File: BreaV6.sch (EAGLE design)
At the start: 34 parts, among them J1 XF2L-0535-1, J2 XF2L-0535-1, Q1 ABM-16MHZ, SW1 LS12T2-T, SW2 EVQ11U09K, SW3 ESE31L11T, U2 TPS62200, X1 22-23-2021

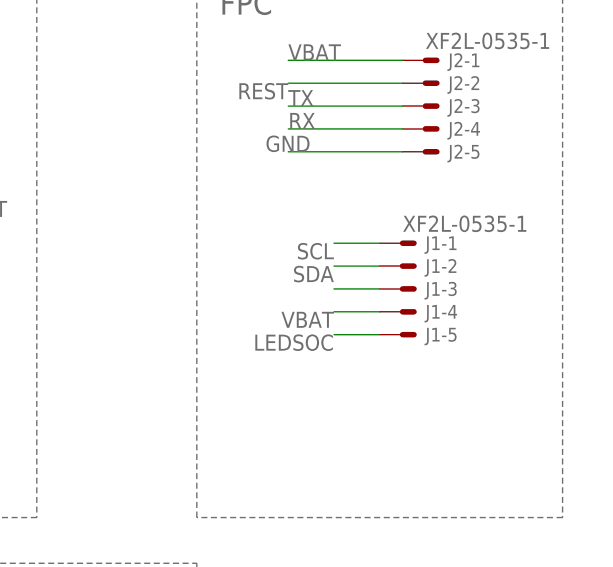
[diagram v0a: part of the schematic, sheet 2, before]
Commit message: Brea V6   PwrSW and DetSW swap
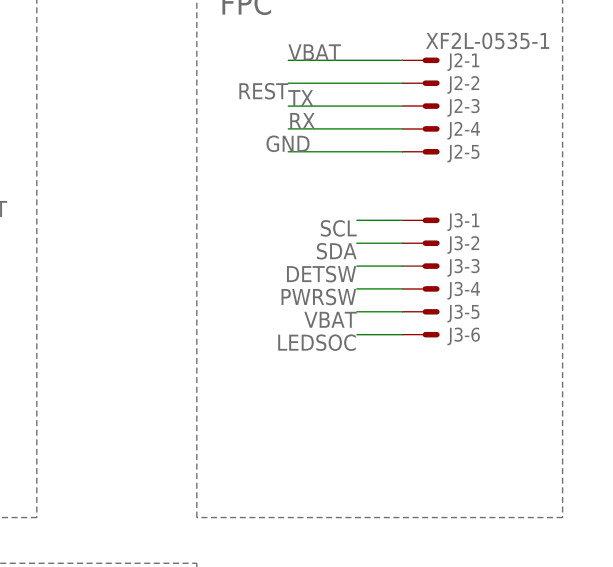
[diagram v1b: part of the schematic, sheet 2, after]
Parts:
- removed J1: XF2L-0535-1, adafruit:XF2L-0535-1
- added J3: XF2L-0635-1, con-omron:XF2L-0635-1
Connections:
- removed net N$6: J1-3.MS
- net DETSW: now also J3-3.MS, U1.PD2(INT0)
- net LEDSOC: now also J3-6.MS; no longer J1-5.MS
- net PWRSW: now also J3-4.MS, U1.PD3(INT1); no longer U1.PD2(INT0)
- net SCL: now also J3-1.MS; no longer J1-1.MSV
- net SDA: now also J3-2.MS; no longer J1-2.MS
- net VBAT: now also J3-5.MS; no longer J1-4.MS
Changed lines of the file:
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@@
 <part name="J2" library="adafruit" deviceset="XF2*-05?" device="35-1" technology="L"/>
 <part name="X1" library="con-molex" deviceset="22-23-2021" device=""/>
-<part name="J1" library="adafruit" deviceset="XF2*-05?" device="35-1" technology="L"/>
 <part name="SW3" library="NewPart" deviceset="ESE31L11T" device=""/>
 <part name="SW2" library="NewPart" deviceset="EVQ11U09K" device=""/>
@@
 <part name="D2" library="diode" library_urn="urn:adsk.eagle:library:210" deviceset="DIODE-" device="SOD523" package3d_urn="urn:adsk.eagle:package:43410/1"/>
 <part name="D3" library="diode" library_urn="urn:adsk.eagle:library:210" deviceset="DIODE-" device="SOD523" package3d_urn="urn:adsk.eagle:package:43410/1"/>
+<part name="J3" library="con-omron" library_urn="urn:adsk.eagle:library:167" deviceset="XF2*-06?" device="35-1" package3d_urn="urn:adsk.eagle:package:9024/1" technology="L"/>
 </parts>
 <sheets>
@@
 </segment>
 </net>
-<net name="PWRSW" class="0">
+<net name="LEDSOC" class="0">
+<segment>
+<pinref part="U1" gate="U$1" pin="PD4(XCK/T0)"/>
+<wire x1="86.36" y1="48.26" x2="91.44" y2="48.26" width="0.1524" layer="91"/>
+<label x="91.44" y="48.26" size="1.778" layer="95"/>
+</segment>
+</net>
+<net name="DETSW" class="0">
 <segment>
 <pinref part="U1" gate="U$1" pin="PD2(INT0)"/>
@@
 </segment>
 </net>
-<net name="LEDSOC" class="0">
-<segment>
-<pinref part="U1" gate="U$1" pin="PD4(XCK/T0)"/>
-<wire x1="86.36" y1="48.26" x2="91.44" y2="48.26" width="0.1524" layer="91"/>
-<label x="91.44" y="48.26" size="1.778" layer="95"/>
+<net name="PWRSW" class="0">
+<segment>
+<pinref part="U1" gate="U$1" pin="PD3(INT1)"/>
+<wire x1="86.36" y1="50.8" x2="91.44" y2="50.8" width="0.1524" layer="91"/>
+<label x="91.44" y="50.8" size="1.778" layer="95"/>
 </segment>
 </net>
@@
 <instance part="X1" gate="-1" x="60.96" y="17.78"/>
 <instance part="X1" gate="-2" x="60.96" y="15.24"/>
-<instance part="J1" gate="-1" x="160.02" y="78.74"/>
-<instance part="J1" gate="-2" x="160.02" y="76.2"/>
-<instance part="J1" gate="-3" x="160.02" y="73.66"/>
-<instance part="J1" gate="-4" x="160.02" y="71.12"/>
-<instance part="J1" gate="-5" x="160.02" y="68.58"/>
 <instance part="GND12" gate="1" x="109.22" y="5.08"/>
 <instance part="R7" gate="G$1" x="109.22" y="25.4" rot="R270"/>
@@
 <instance part="D2" gate="G$1" x="15.24" y="27.94"/>
 <instance part="D3" gate="G$1" x="15.24" y="17.78"/>
+<instance part="J3" gate="-1" x="162.56" y="81.28"/>
+<instance part="J3" gate="-2" x="162.56" y="78.74"/>
+<instance part="J3" gate="-3" x="162.56" y="76.2"/>
+<instance part="J3" gate="-4" x="162.56" y="73.66"/>
+<instance part="J3" gate="-5" x="162.56" y="71.12"/>
+<instance part="J3" gate="-6" x="162.56" y="68.58"/>
 </instances>
 <busses>
@@
 <label x="40.64" y="25.4" size="1.778" layer="95"/>
 </segment>
+<segment>
+<pinref part="J3" gate="-4" pin="MS"/>
+<wire x1="160.02" y1="73.66" x2="154.94" y2="73.66" width="0.1524" layer="91"/>
+<label x="154.94" y="73.66" size="1.778" layer="95" rot="R180"/>
+</segment>
 </net>
 <net name="N$5" class="0">
@@
 <label x="147.32" y="96.52" size="1.778" layer="95" rot="R180"/>
 <pinref part="J2" gate="-2" pin="MS"/>
-</segment>
-</net>
-<net name="SDA" class="0">
-<segment>
-<wire x1="157.48" y1="76.2" x2="152.4" y2="76.2" width="0.1524" layer="91"/>
-<label x="152.4" y="76.2" size="1.778" layer="95" rot="R180"/>
-<pinref part="J1" gate="-2" pin="MS"/>
-</segment>
-</net>
-<net name="SCL" class="0">
-<segment>
-<wire x1="157.48" y1="78.74" x2="152.4" y2="78.74" width="0.1524" layer="91"/>
-<label x="152.4" y="78.74" size="1.778" layer="95" rot="R180"/>
-<pinref part="J1" gate="-1" pin="MSV"/>
 </segment>
 </net>
@@
 <label x="109.22" y="30.48" size="1.778" layer="95" rot="R180" xref="yes"/>
 </segment>
+<segment>
+<pinref part="J3" gate="-3" pin="MS"/>
+<wire x1="160.02" y1="76.2" x2="154.94" y2="76.2" width="0.1524" layer="91"/>
+<label x="154.94" y="76.2" size="1.778" layer="95" rot="R180"/>
+</segment>
 </net>
 <net name="RX" class="0">
@@
 <net name="LEDSOC" class="0">
 <segment>
-<pinref part="J1" gate="-5" pin="MS"/>
-<wire x1="157.48" y1="68.58" x2="152.4" y2="68.58" width="0.1524" layer="91"/>
-<label x="152.4" y="68.58" size="1.778" layer="95" rot="R180"/>
+<pinref part="J3" gate="-6" pin="MS"/>
+<wire x1="160.02" y1="68.58" x2="154.94" y2="68.58" width="0.1524" layer="91"/>
+<label x="154.94" y="68.58" size="1.778" layer="95" rot="R180"/>
 </segment>
 </net>
 <net name="VBAT" class="0">
-<segment>
-<pinref part="J1" gate="-4" pin="MS"/>
-<wire x1="157.48" y1="71.12" x2="152.4" y2="71.12" width="0.1524" layer="91"/>
-<label x="152.4" y="71.12" size="1.778" layer="95" rot="R180"/>
-</segment>
 <segment>
 <pinref part="J2" gate="-1" pin="MSV"/>
@@
 <wire x1="12.7" y1="17.78" x2="7.62" y2="17.78" width="0.1524" layer="91"/>
 <label x="7.62" y="17.78" size="1.778" layer="95" rot="R180" xref="yes"/>
+</segment>
+<segment>
+<pinref part="J3" gate="-5" pin="MS"/>
+<wire x1="160.02" y1="71.12" x2="154.94" y2="71.12" width="0.1524" layer="91"/>
+<label x="154.94" y="71.12" size="1.778" layer="95" rot="R180"/>
 </segment>
 </net>
@@
 </segment>
 </net>
-<net name="N$6" class="0">
-<segment>
-<pinref part="J1" gate="-3" pin="MS"/>
-<wire x1="157.48" y1="73.66" x2="152.4" y2="73.66" width="0.1524" layer="91"/>
-</segment>
-</net>
+<net name="SCL" class="0">
+<segment>
+<pinref part="J3" gate="-1" pin="MS"/>
+<wire x1="160.02" y1="81.28" x2="154.94" y2="81.28" width="0.1524" layer="91"/>
+<label x="154.94" y="81.28" size="1.778" layer="95" rot="R180"/>
+</segment>
+</net>
+<net name="SDA" class="0">
+<segment>
+<pinref part="J3" gate="-2" pin="MS"/>
+<wire x1="160.02" y1="78.74" x2="154.94" y2="78.74" width="0.1524" layer="91"/>
+<label x="154.94" y="78.74" size="1.778" layer="95" rot="R180"/>
+</segment>
+</net>

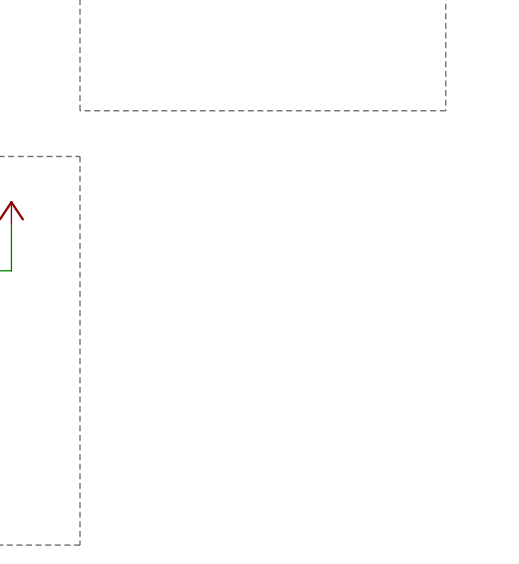
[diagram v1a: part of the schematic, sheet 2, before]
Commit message: To add signal control
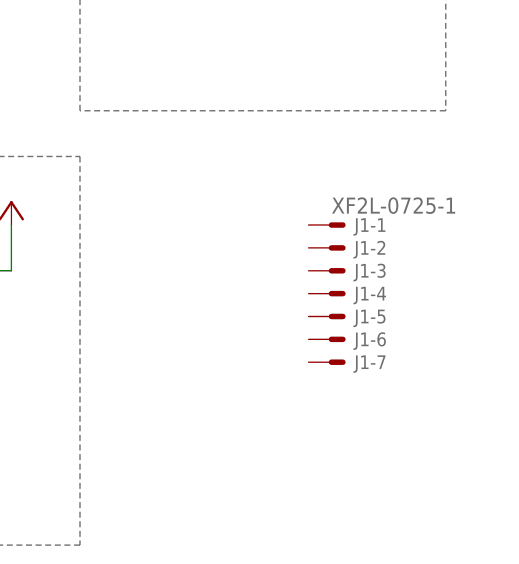
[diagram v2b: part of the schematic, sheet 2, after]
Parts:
- added J1: XF2L-0725-1, con-omron:XF2L-0725-1
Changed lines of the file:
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@@
 <part name="D3" library="diode" library_urn="urn:adsk.eagle:library:210" deviceset="DIODE-" device="SOD523" package3d_urn="urn:adsk.eagle:package:43410/1"/>
 <part name="J3" library="con-omron" library_urn="urn:adsk.eagle:library:167" deviceset="XF2*-06?" device="35-1" package3d_urn="urn:adsk.eagle:package:9024/1" technology="L"/>
+<part name="J1" library="con-omron" library_urn="urn:adsk.eagle:library:167" deviceset="XF2*-07?" device="25-1" package3d_urn="urn:adsk.eagle:package:9008/1" technology="L"/>
 </parts>
 <sheets>
@@
 <instance part="J3" gate="-5" x="162.56" y="71.12"/>
 <instance part="J3" gate="-6" x="162.56" y="68.58"/>
+<instance part="J1" gate="-1" x="165.1" y="35.56"/>
+<instance part="J1" gate="-2" x="165.1" y="33.02"/>
+<instance part="J1" gate="-3" x="165.1" y="30.48"/>
+<instance part="J1" gate="-4" x="165.1" y="27.94"/>
+<instance part="J1" gate="-5" x="165.1" y="25.4"/>
+<instance part="J1" gate="-6" x="165.1" y="22.86"/>
+<instance part="J1" gate="-7" x="165.1" y="20.32"/>
 </instances>
 <busses>

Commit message: Final board files
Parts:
- removed J1: XF2L-0725-1, con-omron:XF2L-0725-1
- added X2: CON-1PINB, NewPart:CON-1PINB
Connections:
- new net SHUTDOWN_SIG: J3-6.MS, U1.PD4(XCK/T0)
- net LEDSOC: now also U1.PD5(T1), X2.P$1; no longer J3-6.MS, U1.PD4(XCK/T0)
- net REST: now also U1.PD6(AIN0); no longer U1.PD5(T1)
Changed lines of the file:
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@@
 <part name="D3" library="diode" library_urn="urn:adsk.eagle:library:210" deviceset="DIODE-" device="SOD523" package3d_urn="urn:adsk.eagle:package:43410/1"/>
 <part name="J3" library="con-omron" library_urn="urn:adsk.eagle:library:167" deviceset="XF2*-06?" device="35-1" package3d_urn="urn:adsk.eagle:package:9024/1" technology="L"/>
-<part name="J1" library="con-omron" library_urn="urn:adsk.eagle:library:167" deviceset="XF2*-07?" device="25-1" package3d_urn="urn:adsk.eagle:package:9008/1" technology="L"/>
+<part name="X2" library="NewPart" deviceset="CON-1PINB" device=""/>
 </parts>
 <sheets>
@@
 </segment>
 </net>
-<net name="REST" class="0">
-<segment>
-<pinref part="U1" gate="U$1" pin="PD5(T1)"/>
-<wire x1="86.36" y1="45.72" x2="93.98" y2="45.72" width="0.1524" layer="91"/>
-<label x="93.98" y="45.72" size="1.778" layer="95"/>
-</segment>
-</net>
 <net name="RX" class="0">
 <segment>
@@
 </segment>
 </net>
-<net name="LEDSOC" class="0">
+<net name="SHUTDOWN_SIG" class="0">
 <segment>
 <pinref part="U1" gate="U$1" pin="PD4(XCK/T0)"/>
@@
 <wire x1="86.36" y1="50.8" x2="91.44" y2="50.8" width="0.1524" layer="91"/>
 <label x="91.44" y="50.8" size="1.778" layer="95"/>
+</segment>
+</net>
+<net name="REST" class="0">
+<segment>
+<pinref part="U1" gate="U$1" pin="PD6(AIN0)"/>
+<wire x1="86.36" y1="43.18" x2="91.44" y2="43.18" width="0.1524" layer="91"/>
+<label x="91.44" y="43.18" size="1.778" layer="95"/>
+</segment>
+</net>
+<net name="LEDSOC" class="0">
+<segment>
+<pinref part="U1" gate="U$1" pin="PD5(T1)"/>
+<wire x1="86.36" y1="45.72" x2="91.44" y2="45.72" width="0.1524" layer="91"/>
+<label x="91.44" y="45.72" size="1.778" layer="95"/>
 </segment>
 </net>
@@
 <instance part="J3" gate="-5" x="162.56" y="71.12"/>
 <instance part="J3" gate="-6" x="162.56" y="68.58"/>
-<instance part="J1" gate="-1" x="165.1" y="35.56"/>
-<instance part="J1" gate="-2" x="165.1" y="33.02"/>
-<instance part="J1" gate="-3" x="165.1" y="30.48"/>
-<instance part="J1" gate="-4" x="165.1" y="27.94"/>
-<instance part="J1" gate="-5" x="165.1" y="25.4"/>
-<instance part="J1" gate="-6" x="165.1" y="22.86"/>
-<instance part="J1" gate="-7" x="165.1" y="20.32"/>
+<instance part="X2" gate="G$1" x="165.1" y="58.42"/>
 </instances>
 <busses>
@@
 </segment>
 </net>
-<net name="LEDSOC" class="0">
+<net name="SHUTDOWN_SIG" class="0">
 <segment>
 <pinref part="J3" gate="-6" pin="MS"/>
@@
 </segment>
 </net>
+<net name="LEDSOC" class="0">
+<segment>
+<pinref part="X2" gate="G$1" pin="P$1"/>
+<wire x1="160.02" y1="58.42" x2="152.4" y2="58.42" width="0.1524" layer="91"/>
+<label x="152.4" y="58.42" size="1.778" layer="95" rot="R180"/>
+</segment>
+</net>
